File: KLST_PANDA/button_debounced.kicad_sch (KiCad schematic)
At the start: 4 parts, among them SW5 BUTTON

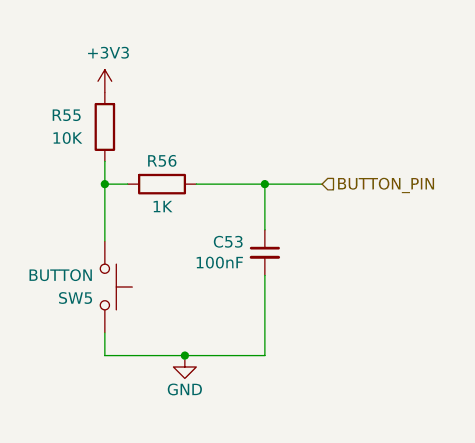
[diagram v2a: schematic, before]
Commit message: started cleaning up schematic ( addressing DRC errors/warning ) (WIP)
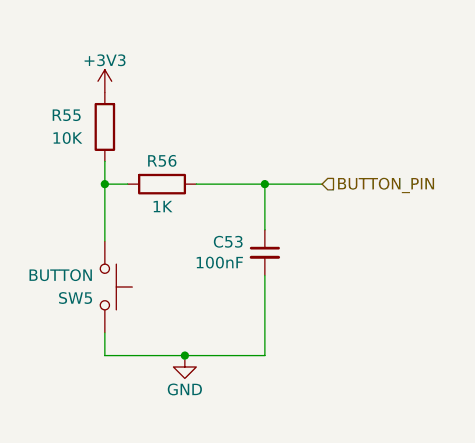
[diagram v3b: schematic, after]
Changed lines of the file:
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@@
       (project "KLST_PANDA"
         (path "/b4513875-4c57-4720-bcc5-43ead67fe18f/f08ee185-46fd-4c64-8c0d-73017bc497ee/7936a5e0-5a04-43e4-aa84-42432289d154"
-          (reference "#PWR067") (unit 1)
+          (reference "#PWR068") (unit 1)
         )
       )
@@
       (effects (font (size 1.27 1.27)) hide)
     )
-    (property "Value" "+3V3" (at 138.811 84.5058 0)
+    (property "Value" "+3V3" (at 138.43 85.344 0)
       (effects (font (size 1.27 1.27)))
     )
@@
       (project "KLST_PANDA"
         (path "/b4513875-4c57-4720-bcc5-43ead67fe18f/f08ee185-46fd-4c64-8c0d-73017bc497ee/7936a5e0-5a04-43e4-aa84-42432289d154"
-          (reference "#PWR066") (unit 1)
+          (reference "#PWR067") (unit 1)
         )
       )

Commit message: removed DRC warnings and error, added power page
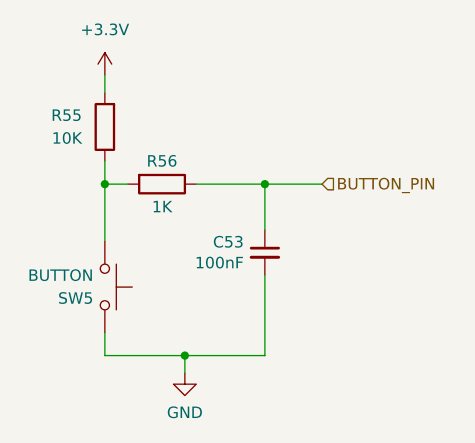
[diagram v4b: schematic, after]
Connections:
- net +3V3 renamed +3.3V
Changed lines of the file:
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@@
   (junction (at 156.21 99.06) (diameter 0) (color 0 0 0 0)
   )
+  (wire (pts (xy 138.43 86.995) (xy 138.43 88.9))
+    (stroke (width 0) (type default))
+  )
   (wire (pts (xy 138.43 99.06) (xy 138.43 105.41))
     (stroke (width 0) (type default))
@@
     (stroke (width 0) (type default))
   )
+  (wire (pts (xy 147.32 118.11) (xy 147.32 120.015))
+    (stroke (width 0) (type default))
+  )
   (wire (pts (xy 138.43 96.52) (xy 138.43 99.06))
     (stroke (width 0) (type default))
@@
     (stroke (width 0) (type default))
   )
+  (wire (pts (xy 147.32 118.11) (xy 156.21 118.11))
+    (stroke (width 0) (type default))
+  )
   (wire (pts (xy 138.43 118.11) (xy 147.32 118.11))
-    (stroke (width 0) (type default))
-  )
-  (wire (pts (xy 147.32 118.11) (xy 156.21 118.11))
     (stroke (width 0) (type default))
   )
@@
       (project "KLST_PANDA"
         (path "/b4513875-4c57-4720-bcc5-43ead67fe18f/f08ee185-46fd-4c64-8c0d-73017bc497ee/7936a5e0-5a04-43e4-aa84-42432289d154"
-          (reference "R49") (unit 1)
-        )
-      )
-    )
-  )
-  (symbol (lib_id "power:GND") (at 147.32 118.11 0) (unit 1)
-    (in_bom yes) (on_board yes) (dnp no)
-    (property "Reference" "#PWR081" (at 147.32 124.46 0)
-      (effects (font (size 1.27 1.27)) hide)
-    )
-    (property "Value" "GND" (at 147.32 121.92 0)
-      (effects (font (size 1.27 1.27)))
-    )
-    (property "Footprint" "" (at 147.32 118.11 0)
-      (effects (font (size 1.27 1.27)) hide)
-    )
-    (property "Datasheet" "" (at 147.32 118.11 0)
-      (effects (font (size 1.27 1.27)) hide)
-    )
-    (pin "1")
-    (instances
-      (project "KLST_SHEEP"
-        (path "/7c1fd6fc-5c53-4ccb-a456-46fe6fc0bc71/00000000-0000-0000-0000-00006058fda0"
-          (reference "#PWR081") (unit 1)
-        )
-      )
-      (project "KLST_PANDA"
-        (path "/b4513875-4c57-4720-bcc5-43ead67fe18f/f08ee185-46fd-4c64-8c0d-73017bc497ee/7936a5e0-5a04-43e4-aa84-42432289d154"
-          (reference "#PWR068") (unit 1)
-        )
-      )
-    )
-  )
-  (symbol (lib_id "power:+3V3") (at 138.43 88.9 0) (unit 1)
-    (in_bom yes) (on_board yes) (dnp no)
-    (property "Reference" "#PWR080" (at 138.43 92.71 0)
-      (effects (font (size 1.27 1.27)) hide)
-    )
-    (property "Value" "+3V3" (at 138.43 85.344 0)
-      (effects (font (size 1.27 1.27)))
-    )
-    (property "Footprint" "" (at 138.43 88.9 0)
-      (effects (font (size 1.27 1.27)) hide)
-    )
-    (property "Datasheet" "" (at 138.43 88.9 0)
-      (effects (font (size 1.27 1.27)) hide)
-    )
-    (pin "1")
-    (instances
-      (project "KLST_SHEEP"
-        (path "/7c1fd6fc-5c53-4ccb-a456-46fe6fc0bc71/00000000-0000-0000-0000-00006058fda0"
-          (reference "#PWR080") (unit 1)
-        )
-      )
-      (project "KLST_PANDA"
-        (path "/b4513875-4c57-4720-bcc5-43ead67fe18f/f08ee185-46fd-4c64-8c0d-73017bc497ee/7936a5e0-5a04-43e4-aa84-42432289d154"
-          (reference "#PWR067") (unit 1)
+          (reference "R35") (unit 1)
+        )
+      )
+    )
+  )
+  (symbol (lib_id "power:+3.3V") (at 138.43 86.995 0) (unit 1)
+    (in_bom yes) (on_board yes) (dnp no) (fields_autoplaced)
+    (property "Reference" "#PWR077" (at 138.43 90.805 0)
+      (effects (font (size 1.27 1.27)) hide)
+    )
+    (property "Value" "+3.3V" (at 138.43 81.915 0)
+      (effects (font (size 1.27 1.27)))
+    )
+    (property "Footprint" "" (at 138.43 86.995 0)
+      (effects (font (size 1.27 1.27)) hide)
+    )
+    (property "Datasheet" "" (at 138.43 86.995 0)
+      (effects (font (size 1.27 1.27)) hide)
+    )
+    (pin "1")
+    (instances
+      (project "KLST_PANDA"
+        (path "/b4513875-4c57-4720-bcc5-43ead67fe18f/47e8e77e-c64e-4c44-bfd8-2073580a3d85"
+          (reference "#PWR077") (unit 1)
+        )
+        (path "/b4513875-4c57-4720-bcc5-43ead67fe18f/f08ee185-46fd-4c64-8c0d-73017bc497ee/7936a5e0-5a04-43e4-aa84-42432289d154"
+          (reference "#PWR060") (unit 1)
         )
       )
@@
       (project "KLST_PANDA"
         (path "/b4513875-4c57-4720-bcc5-43ead67fe18f/f08ee185-46fd-4c64-8c0d-73017bc497ee/7936a5e0-5a04-43e4-aa84-42432289d154"
-          (reference "C66") (unit 1)
+          (reference "C42") (unit 1)
         )
       )
@@
       (project "KLST_PANDA"
         (path "/b4513875-4c57-4720-bcc5-43ead67fe18f/f08ee185-46fd-4c64-8c0d-73017bc497ee/7936a5e0-5a04-43e4-aa84-42432289d154"
-          (reference "R48") (unit 1)
-        )
-      )
+          (reference "R34") (unit 1)
+        )
+      )
+    )
+  )
+  (symbol (lib_id "power:GND") (at 147.32 120.015 0) (unit 1)
+    (in_bom yes) (on_board yes) (dnp no) (fields_autoplaced)
+    (property "Reference" "#PWR061" (at 147.32 126.365 0)
+      (effects (font (size 1.27 1.27)) hide)
+    )
+    (property "Value" "GND" (at 147.32 124.46 0)
+      (effects (font (size 1.27 1.27)))
+    )
+    (property "Footprint" "" (at 147.32 120.015 0)
+      (effects (font (size 1.27 1.27)) hide)
+    )
+    (property "Datasheet" "" (at 147.32 120.015 0)
+      (effects (font (size 1.27 1.27)) hide)
+    )
+    (pin "1")
+    (instances
+      (project "KLST_PANDA"
+        (path "/b4513875-4c57-4720-bcc5-43ead67fe18f/f08ee185-46fd-4c64-8c0d-73017bc497ee/7936a5e0-5a04-43e4-aa84-42432289d154"
+          (reference "#PWR061") (unit 1)
+        )
+      )
